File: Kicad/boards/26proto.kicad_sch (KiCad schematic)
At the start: 31 parts, among them J1 5051104096, J2 Micro_SD_Card, J3 URM37, J4 RE12A, J5 RS485_TFT, J6 RS485_airdata, J7 RS485_logger_2, J8 RS485_logger, J9 BNO085, Q2 NPN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

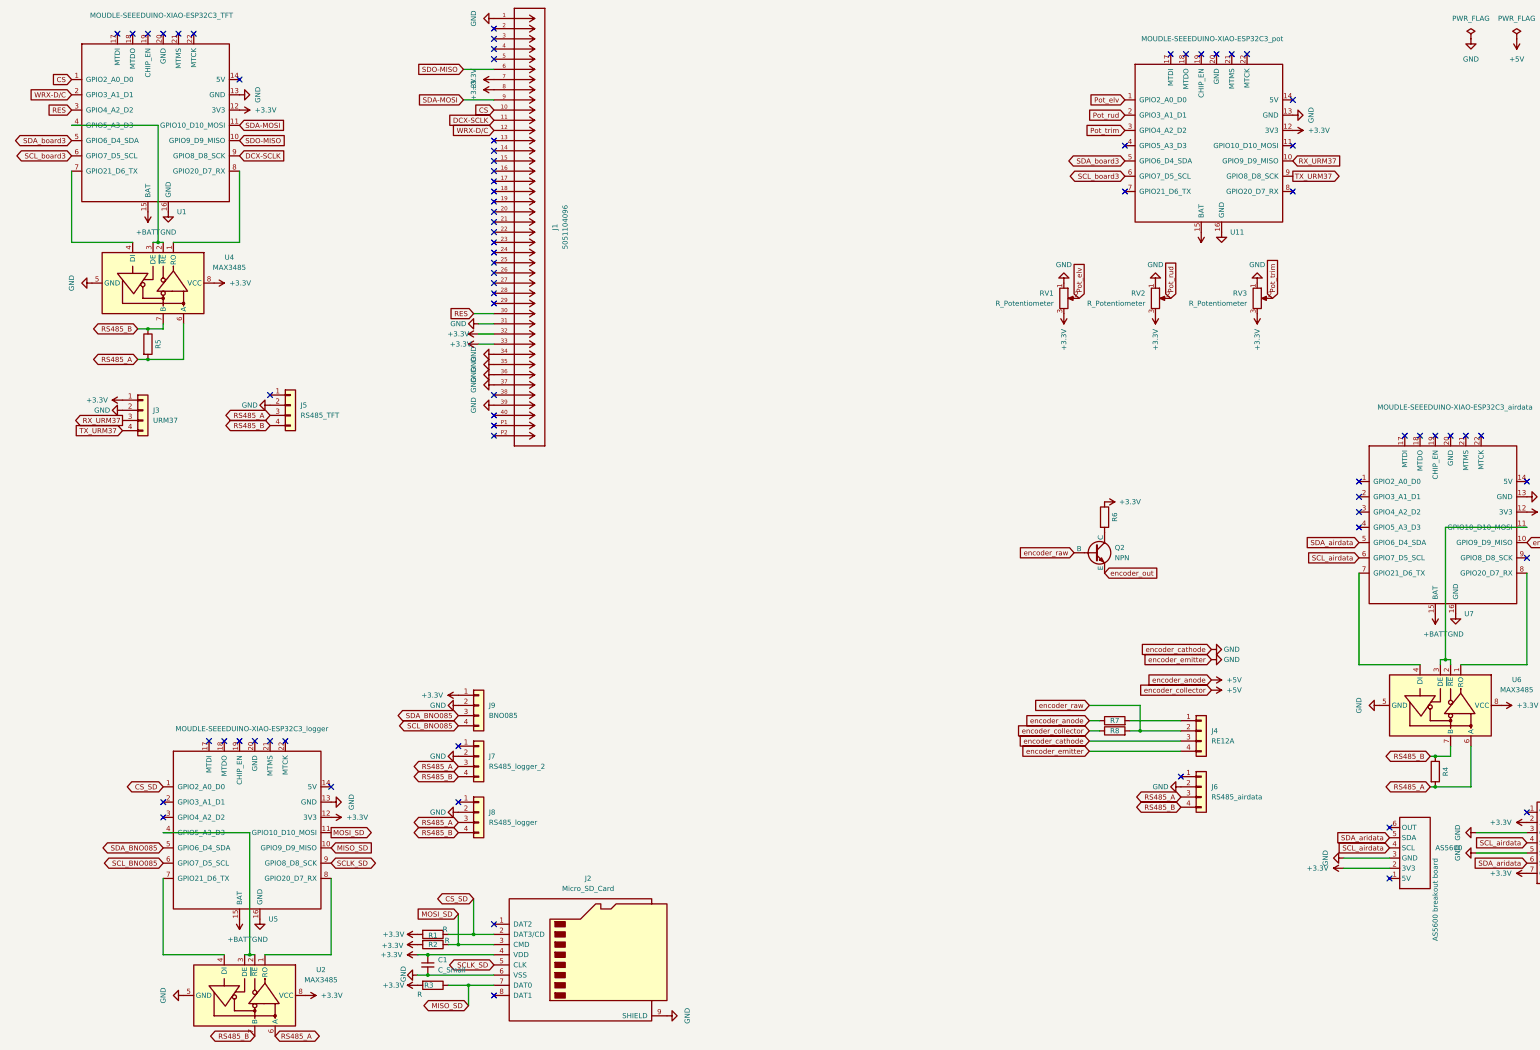
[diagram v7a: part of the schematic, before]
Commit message: Add battery connector and update net assignments
Added Batt1 JST PH connector footprint and R4 resistor for RS485 lines. Updated net assignments for U11 pins, replaced encoder_anode with +3.3V and pot_Vin where appropriate, and made related schematic and PCB changes. Also added a backup ZIP file.
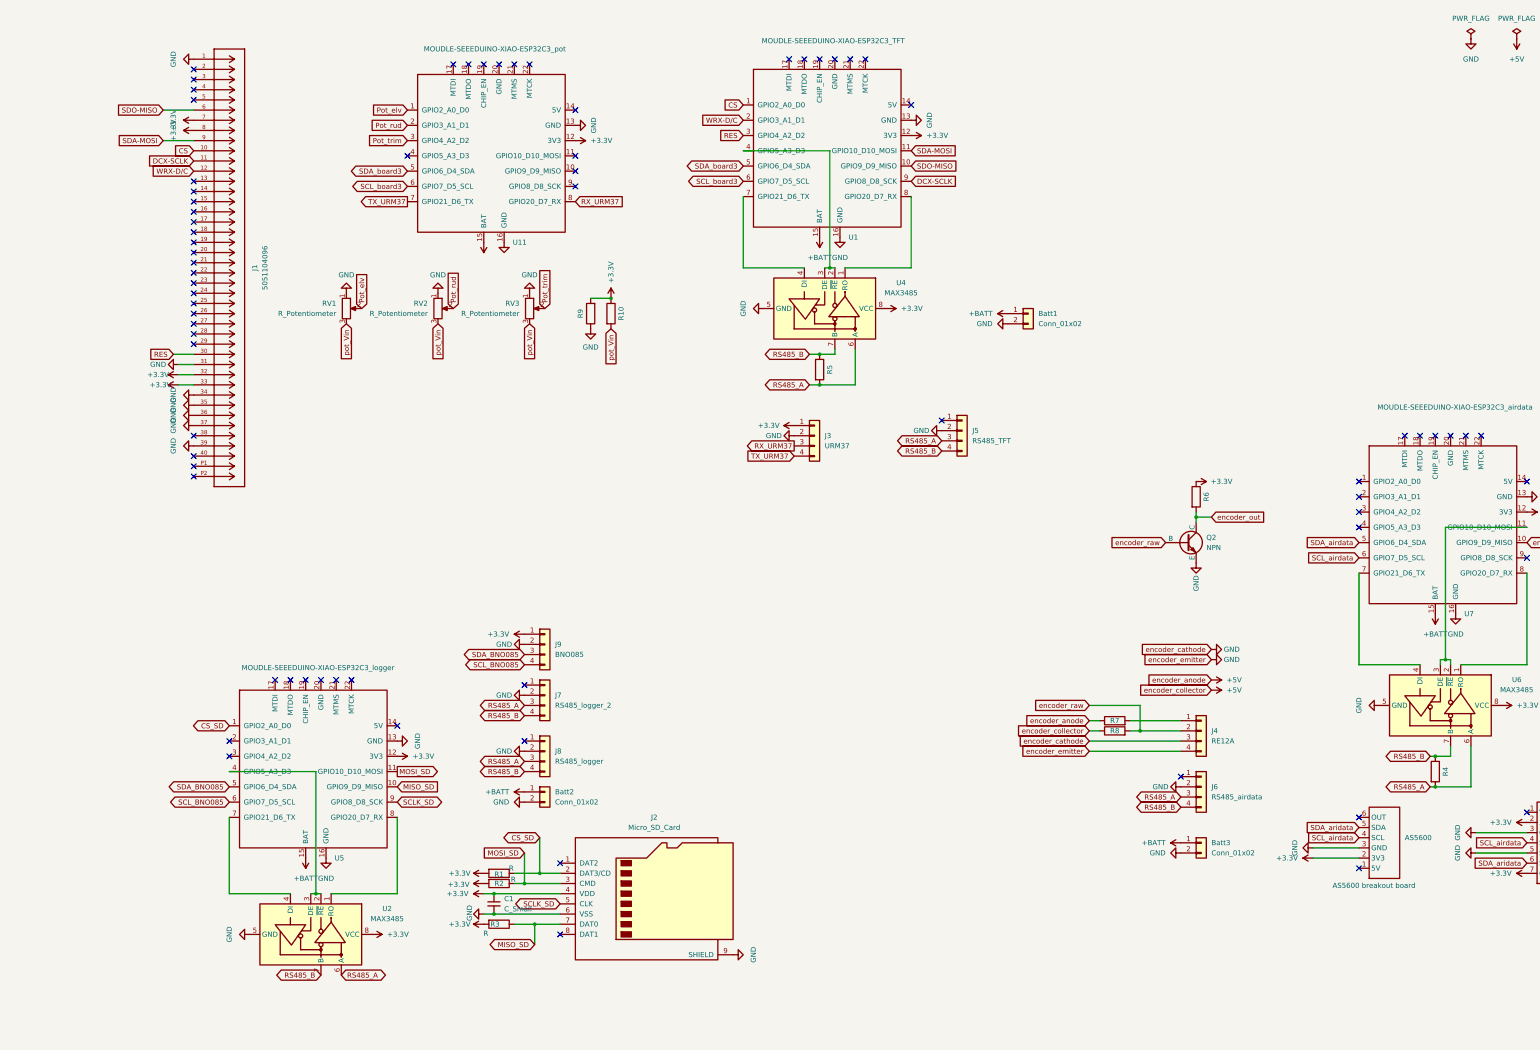
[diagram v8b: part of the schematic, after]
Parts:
- added Batt1, Batt2, Batt3: Conn_01x02, Connector_JST:JST_PH_S2B-PH-SM4-TB_1x02-1MP_P2.00mm_Horizontal, symbol Connector_Generic:Conn_01x02
- added R10, R9: R, Resistor_SMD:R_0201_0603Metric_Pad0.64x0.40mm_HandSolder, symbol Device:R
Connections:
- net +3.3V: now also R10.1, R9.2; no longer RV1.3, RV2.3, RV3.3
- net +BATT: now also Batt1.1 (Pin_1), Batt2.1 (Pin_1), Batt3.1 (Pin_1)
- net GND: now also Q2.3 (E), Batt1.2 (Pin_2), Batt2.2 (Pin_2), Batt3.2 (Pin_2), R9.1
- net RX_URM37: now also U11.8 (GPIO20_D7_RX); no longer U11.10 (GPIO9_D9_MISO)
- net TX_URM37: now also U11.7 (GPIO21_D6_TX); no longer U11.9 (GPIO8_D8_SCK)
- net encoder_out: now also Q2.1 (C), R6.2; no longer Q2.3 (E)
- new net pot_Vin: R10.2, RV1.3, RV2.3, RV3.3
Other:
- moved on the sheet: AS5600, C1, J1, J2, J3, J5, J7, J8, J9, Q2, R1, R2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
